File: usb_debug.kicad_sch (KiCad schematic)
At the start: 12 parts, among them J10 SWD header 1x03 2.54 mm (SWCL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, J4 USB_C_PROGRAM_POWER

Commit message: update
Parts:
- J10: now in the parts list
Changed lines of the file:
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@@
 		(body_style 1)
 		(exclude_from_sim no)
-		(in_bom no)
+		(in_bom yes)
 		(on_board yes)
-		(in_pos_files no)
+		(in_pos_files yes)
 		(dnp no)
 		(property "Reference" "J10"

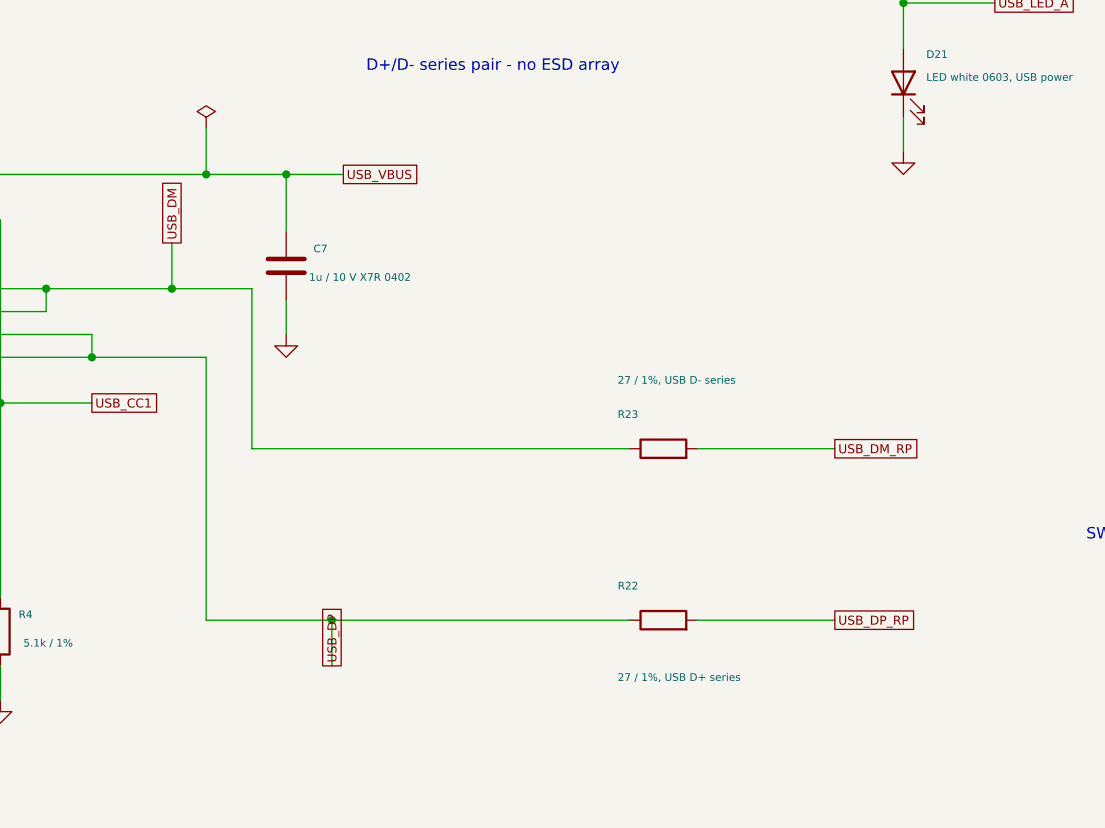
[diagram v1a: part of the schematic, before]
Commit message: finished routing reg, gp under sd & flash, icm solder mask exclusion
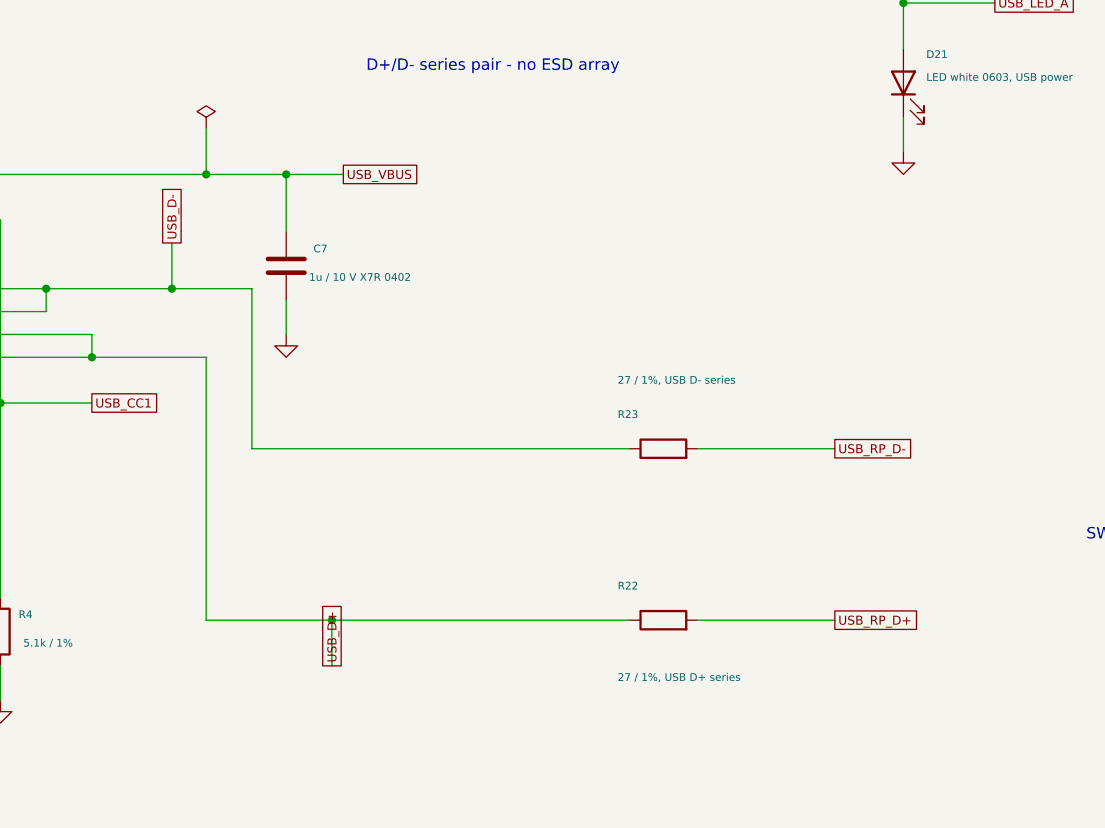
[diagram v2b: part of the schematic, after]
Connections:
- net USB_DM renamed USB_D-
- net USB_DM_RP renamed USB_RP_D-
- net USB_DP renamed USB_D+
- net USB_DP_RP renamed USB_RP_D+
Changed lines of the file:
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@@
 		)
 	)
-	(global_label "USB_DM_RP"
+	(global_label "USB_RP_D-"
 		(shape passive)
 		(at 168.91 104.14 0)
@@
 		)
 	)
-	(global_label "USB_DM"
+	(global_label "USB_D-"
 		(shape passive)
 		(at 95.25 81.28 90)
@@
 		)
 	)
-	(global_label "USB_DP"
+	(global_label "USB_D+"
 		(shape passive)
 		(at 113.03 128.27 90)
@@
 		)
 	)
-	(global_label "USB_DP_RP"
+	(global_label "USB_RP_D+"
 		(shape passive)
 		(at 168.91 123.19 0)
